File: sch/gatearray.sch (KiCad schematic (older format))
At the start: 78 parts, among them X2 CONN-7S

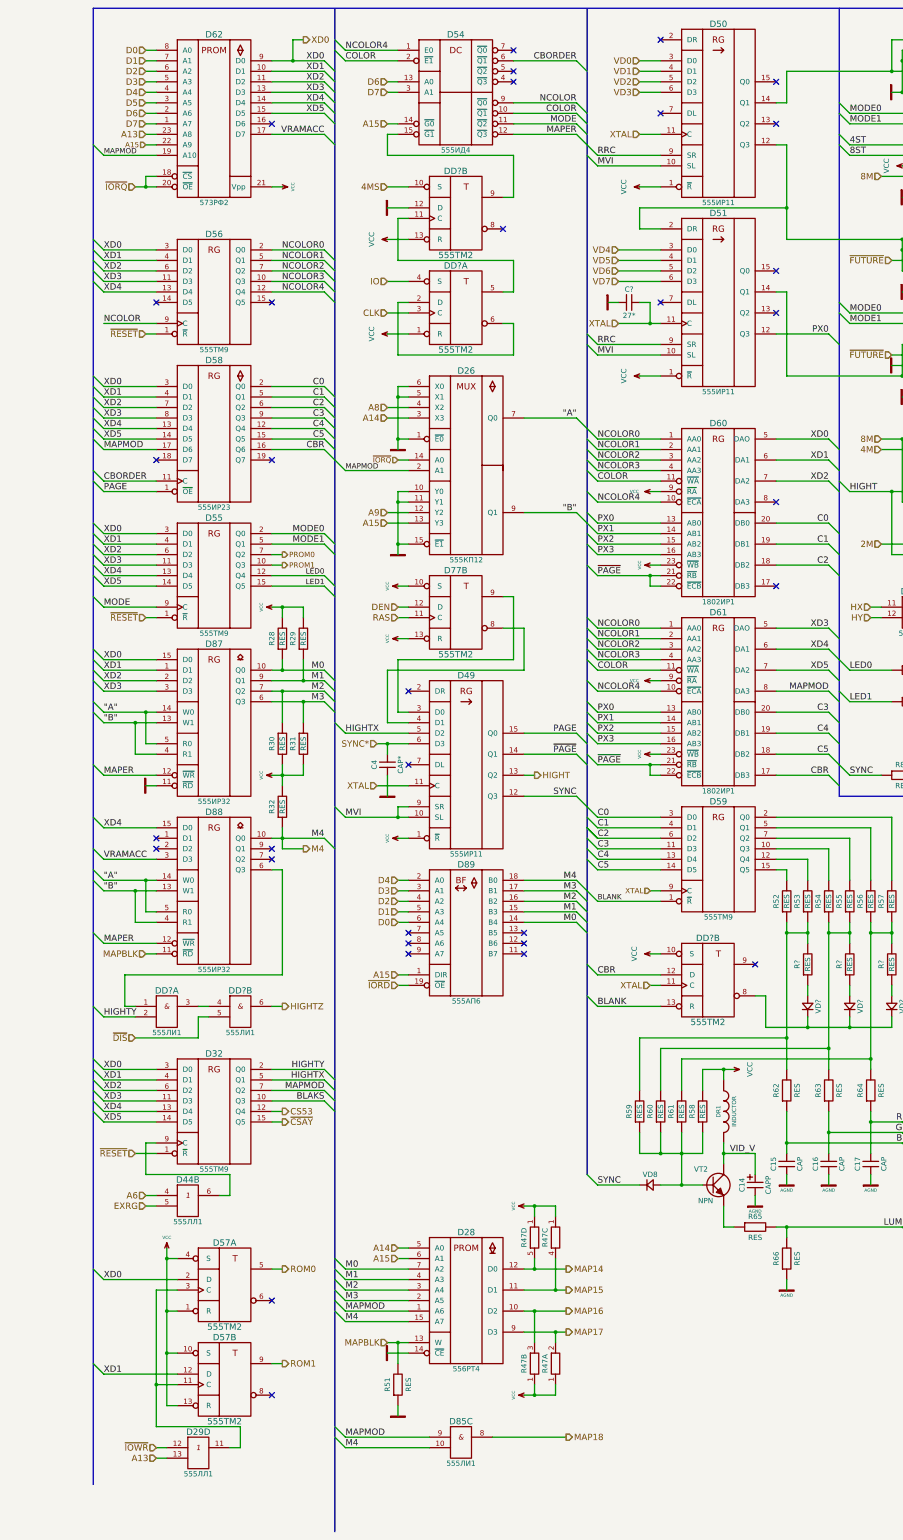
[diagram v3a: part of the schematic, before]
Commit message: Another ROM replaced with PLD, source included
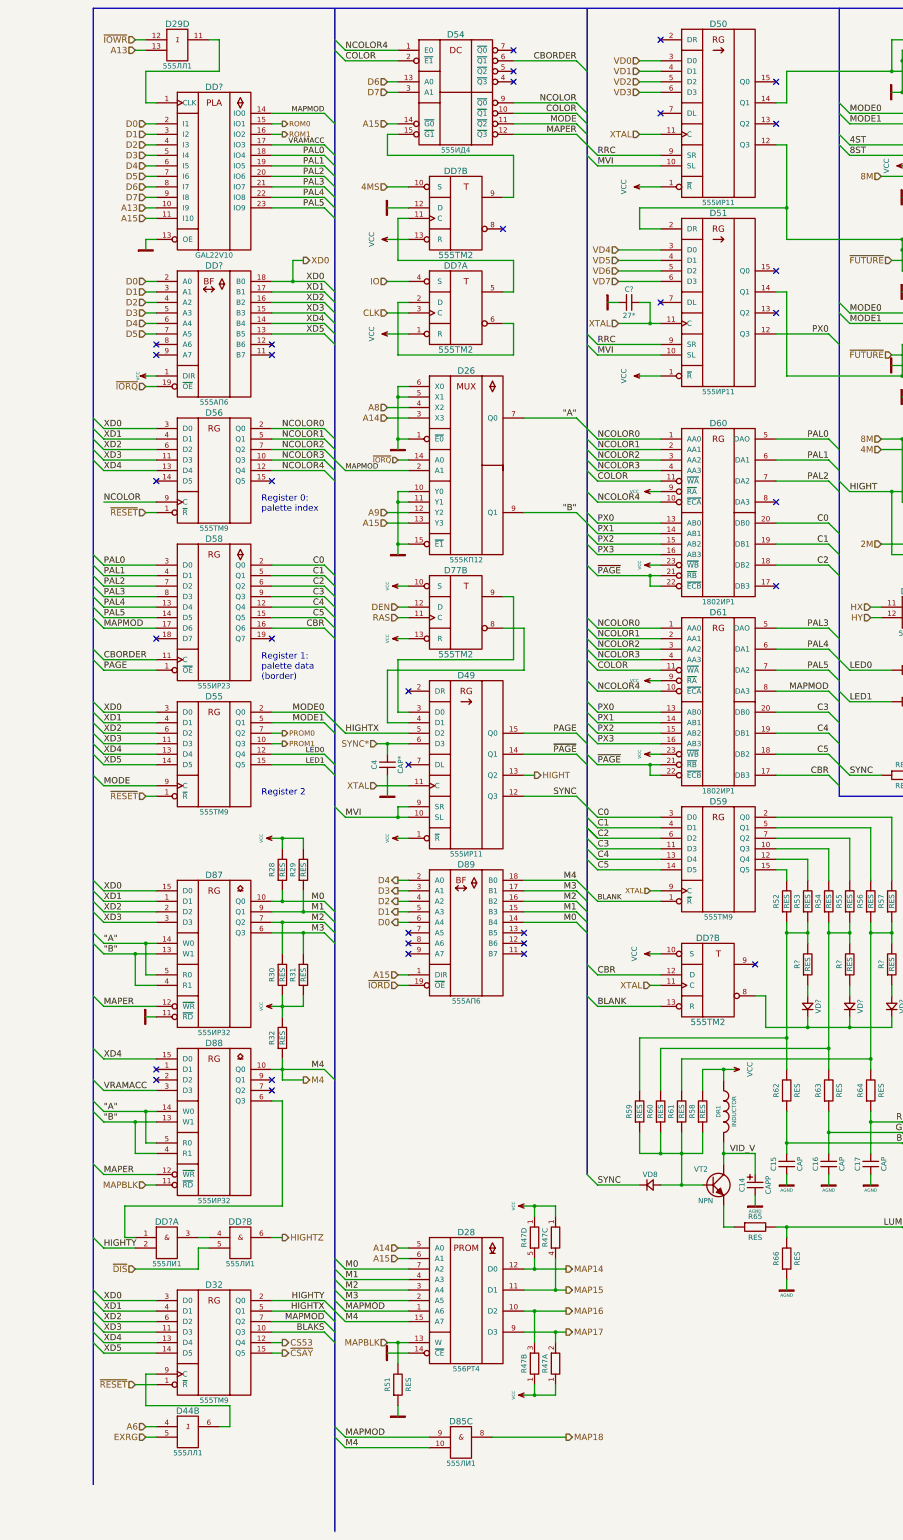
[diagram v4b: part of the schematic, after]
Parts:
- removed D57: 555ТМ2, MyLib:DIP-14, symbol 555ТМ2
- removed D62: 573РФ2, MyLib:DIP-24, symbol 573РФ2
- added DD?: GAL22V10, symbol GAL22V10
- added DD?: 555АП6, symbol 555АП6
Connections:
- net A13: now also DD?.10 (I9)
- net A15: now also DD?.11 (I10)
- net D0: now also DD?.2 (A0), DD?.2 (I1)
- net D1: now also DD?.3 (A1), DD?.3 (I2)
- net D2: now also DD?.4 (A2), DD?.4 (I3)
- net D3: now also DD?.5 (A3), DD?.5 (I4)
- net D4: now also DD?.6 (A4), DD?.6 (I5)
- net D5: now also DD?.7 (A5), DD?.7 (I6)
- net D6: now also DD?.8 (I7)
- net D7: now also DD?.9 (I8)
- net GND: now also DD?.10 (GND), DD?.12 (GND), DD?.13 (OE)
- net MAPMOD: now also DD?.14 (IO0)
- net ROM0: now also DD?.15 (IO1)
- net ROM1: now also DD?.16 (IO2)
- net VCC: now also DD?.1 (DIR), DD?.20 (VCC), DD?.24 (VCC)
- net VRAMACC: now also DD?.17 (IO3)
- net XD0: now also DD?.18 (B0); no longer D58.3 (D0), D60.5 (DAO)
- net XD1: now also DD?.17 (B1); no longer D58.4 (D1), D60.6 (DA1)
- net XD2: now also DD?.16 (B2); no longer D58.7 (D2), D60.7 (DA2)
- net XD3: now also DD?.15 (B3); no longer D58.8 (D3), D61.5 (DAO)
- net XD4: now also DD?.14 (B4); no longer D58.13 (D4), D61.6 (DA1)
- net XD5: now also DD?.13 (B5); no longer D58.14 (D5), D61.7 (DA2)
- net ~IORQ: now also DD?.19 (~OE)
- net at D29.11 (out): now also DD?.1 (CLK)
- new net PAL0: D58.3 (D0), D60.5 (DAO), DD?.18 (IO4)
- new net PAL1: D58.4 (D1), D60.6 (DA1), DD?.19 (IO5)
- new net PAL2: D58.7 (D2), D60.7 (DA2), DD?.20 (IO6)
- new net PAL3: D58.8 (D3), D61.5 (DAO), DD?.21 (IO7)
- new net PAL4: D58.13 (D4), D61.6 (DA1), DD?.22 (IO8)
- new net PAL5: D58.14 (D5), D61.7 (DA2), DD?.23 (IO9)
- no-connect marks 33 -> 34
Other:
- note added: "Register 0:\npalette index"
- note added: "Register 1:\npalette data\n(border)\n"
- note added: "Register 2"
- moved on the sheet: D29D, D32, D44B, D55, D56, D58, D87, D88, DD?A, DD?B, R28, R29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

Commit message: Fix MVI signal
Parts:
- added DD?: GAL16V8, symbol GAL16V8
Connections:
- net A14: now also DD?.2 (I1)
- net A15: now also DD?.3 (I2)
- net GND: now also DD?.10 (GND)
- net HIGHTY: now also DD?.12 (IO0)
- net HIGHTZ: now also DD?.14 (IO2)
- net M0: now also DD?.4 (I3)
- net M1: now also DD?.5 (I4)
- net M2: now also DD?.6 (I5)
- net M3: now also DD?.7 (I6)
- net M4: now also DD?.8 (I7)
- net MAP14: now also DD?.19 (IO7)
- net MAP15: now also DD?.18 (IO6)
- net MAP16: now also DD?.17 (IO5)
- net MAP17: now also DD?.16 (IO4)
- net MAP18: now also DD?.15 (IO3)
- net MAPBLK: now also DD?.11 (OE)
- net MAPMOD: now also DD?.9 (I8)
- net VCC: now also DD?.20 (VCC)
- net ~DIS: now also DD?.1 (CLK)
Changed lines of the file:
@@
 Text HLabel 8500 5300 0    60   Input ~ 0
 4M
-Text Label 10400 6100 2    60   ~ 0
-MVI
-Text Label 10400 5700 2    60   ~ 0
+Text Label 10600 5700 2    60   ~ 0
 8ST
-Text Label 10400 5800 2    60   ~ 0
+Text Label 10600 5800 2    60   ~ 0
 4ST
 Text Label 5800 2500 0    60   ~ 0
@@
 Text HLabel 8500 2700 0    60   Input ~ 0
 8M
-Text Label 10400 3600 2    60   ~ 0
+Text Label 10600 3600 2    60   ~ 0
 PX1
-Text Label 10400 4500 2    60   ~ 0
+Text Label 10600 4500 2    60   ~ 0
 PX2
-Text Label 10400 1700 2    60   ~ 0
+Text Label 10600 1700 2    60   ~ 0
 PX3
-Text Label 10400 2600 2    60   ~ 0
+Text Label 10600 2600 2    60   ~ 0
 RRC
 Entry Wire Line
@@
 	8100 2100 8200 2200
 Entry Wire Line
-	10400 1700 10500 1800
-Entry Wire Line
-	10400 2600 10500 2700
-Entry Wire Line
-	10400 3600 10500 3700
-Entry Wire Line
-	10400 4500 10500 4600
+	10600 1700 10700 1800
+Entry Wire Line
+	10600 2600 10700 2700
+Entry Wire Line
+	10600 3600 10700 3700
+Entry Wire Line
+	10600 4500 10700 4600
 Entry Wire Line
 	5700 2400 5800 2500
@@
 	8100 5600 8200 5700
 Entry Wire Line
-	10400 5700 10500 5800
-Entry Wire Line
-	10400 5800 10500 5900
-Entry Wire Line
-	10400 6100 10500 6200
+	10600 5700 10700 5800
+Entry Wire Line
+	10600 5800 10700 5900
 $Comp
 L VCC #PWR060
@@
 $EndComp
 Entry Wire Line
-	10400 6800 10500 6900
-Text Label 10400 6800 2    60   ~ 0
+	10600 6800 10700 6900
+Text Label 10600 6800 2    60   ~ 0
 BLANK
 $Comp
@@
 $EndComp
 Entry Wire Line
-	10400 7000 10500 7100
-Text Label 10400 7000 2    60   ~ 0
+	10600 7000 10700 7100
+Text Label 10600 7000 2    60   ~ 0
 BLAKS
 $Comp
@@
 	9600 6200 9400 6200
 Wire Wire Line
-	9400 5700 10400 5700
-Wire Wire Line
-	10200 6100 10400 6100
+	9400 5700 10600 5700
+Wire Wire Line
+	10200 6100 10600 6100
 Wire Wire Line
 	8500 5200 8800 5200
@@
 Connection ~ 8600 5700
 Wire Wire Line
-	10400 5800 9500 5800
+	10600 5800 9500 5800
 Connection ~ 9500 5800
 Wire Wire Line
@@
 	8500 2700 8800 2700
 Wire Wire Line
-	9900 1700 10400 1700
-Wire Wire Line
-	10400 2600 9900 2600
-Wire Wire Line
-	10400 3600 9900 3600
-Wire Wire Line
-	10400 4500 9900 4500
+	9900 1700 10600 1700
+Wire Wire Line
+	10600 2600 9900 2600
+Wire Wire Line
+	10600 3600 9900 3600
+Wire Wire Line
+	10600 4500 9900 4500
 Wire Bus Line
 	8100 1100 8100 8600
@@
 Connection ~ 8700 4600
 Wire Bus Line
-	10500 1100 10500 8000
+	10700 1100 10700 8000
 Wire Bus Line
 	5700 1100 5700 12200
@@
 	1000 1100 1000 15150
 Wire Bus Line
-	1000 1100 10500 1100
+	1000 1100 10700 1100
 Wire Wire Line
 	8500 6900 8400 6900
@@
 	9200 6800 9100 6800
 Wire Wire Line
-	9400 6800 10400 6800
+	9400 6800 10600 6800
 Wire Wire Line
 	9600 7000 9500 7000
@@
 Connection ~ 9500 6800
 Wire Wire Line
-	10000 7000 10400 7000
+	10000 7000 10600 7000
 Wire Wire Line
 	4800 14700 5500 14700
@@
 	2900 3500 2900 3700
 Connection ~ 2900 3700
+$Comp
+L GAL16V8 DD?
+U 1 1 57CD6B67
+P 4100 16900
+F 0 "DD?" H 4650 17050 60  0000 C CNN
+F 1 "GAL16V8" H 4650 15650 50  0000 C CNN
+F 2 "" H 4400 16650 60  0000 C CNN
+F 3 "" H 4400 16650 60  0000 C CNN
+	1    4100 16900
+	1    0    0    -1
+$EndComp
+Text HLabel 4000 17100 0    60   Input ~ 0
+A14
+Text HLabel 4000 17200 0    60   Input ~ 0
+A15
+Text Label 3500 17300 0    60   ~ 0
+M0
+Text Label 3500 17400 0    60   ~ 0
+M1
+Text Label 3500 17500 0    60   ~ 0
+M2
+Text Label 3500 17600 0    60   ~ 0
+M3
+Text Label 3500 17800 0    60   ~ 0
+MAPMOD
+Text Label 3500 17700 0    60   ~ 0
+M4
+Entry Wire Line
+	3400 17700 3500 17800
+Entry Wire Line
+	3400 17600 3500 17700
+Entry Wire Line
+	3400 17500 3500 17600
+Entry Wire Line
+	3400 17300 3500 17400
+Entry Wire Line
+	3400 17400 3500 17500
+Entry Wire Line
+	3400 17200 3500 17300
+Text HLabel 3900 18000 0    60   Input ~ 0
+MAPBLK
+Wire Wire Line
+	3500 17300 4100 17300
+Wire Wire Line
+	3500 17400 4100 17400
+Wire Wire Line
+	3500 17500 4100 17500
+Wire Wire Line
+	3500 17600 4100 17600
+Wire Wire Line
+	3500 17700 4100 17700
+Wire Wire Line
+	3500 17800 4100 17800
+Wire Wire Line
+	4000 17100 4100 17100
+Wire Wire Line
+	4000 17200 4100 17200
+Wire Wire Line
+	3900 18000 4100 18000
+Text HLabel 5400 17700 2    60   Output ~ 0
+MAP14
+Text HLabel 5400 17600 2    60   Output ~ 0
+MAP15
+Text HLabel 5400 17500 2    60   Output ~ 0
+MAP16
+Text HLabel 5400 17400 2    60   Output ~ 0
+MAP17
+Wire Wire Line
+	5400 17600 5200 17600
+Wire Wire Line
+	5400 17500 5200 17500
+Wire Wire Line
+	5200 17400 5400 17400
+Wire Wire Line
+	5400 17300 5200 17300
+Text Label 5700 17000 2    60   ~ 0
+HIGHTY
+Wire Wire Line
+	5700 17000 5200 17000
+Text HLabel 4000 16900 0    60   Input ~ 0
+~DIS
+Text HLabel 5400 17200 2    60   Output ~ 0
+HIGHTZ
+Wire Wire Line
+	5200 17100 5800 17100
+Wire Wire Line
+	5400 17200 5200 17200
+Text HLabel 5400 17300 2    60   Output ~ 0
+MAP18
+Wire Wire Line
+	5400 17700 5200 17700
+Entry Wire Line
+	5800 16900 5700 17000
+Wire Wire Line
+	4000 16900 4100 16900
+Text HLabel 10400 6300 2    60   Output ~ 0
+MVI
+Entry Wire Line
+	10600 6100 10700 6200
+Text Label 10600 6100 2    60   ~ 0
+MVI
+Wire Wire Line
+	10400 6300 10300 6300
+Wire Wire Line
+	10300 6300 10300 6100
+Connection ~ 10300 6100
 $EndSCHEMATC
